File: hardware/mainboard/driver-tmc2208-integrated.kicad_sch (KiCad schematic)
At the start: 9 parts, among them M1 JST XH, U2 TMC2208-LA

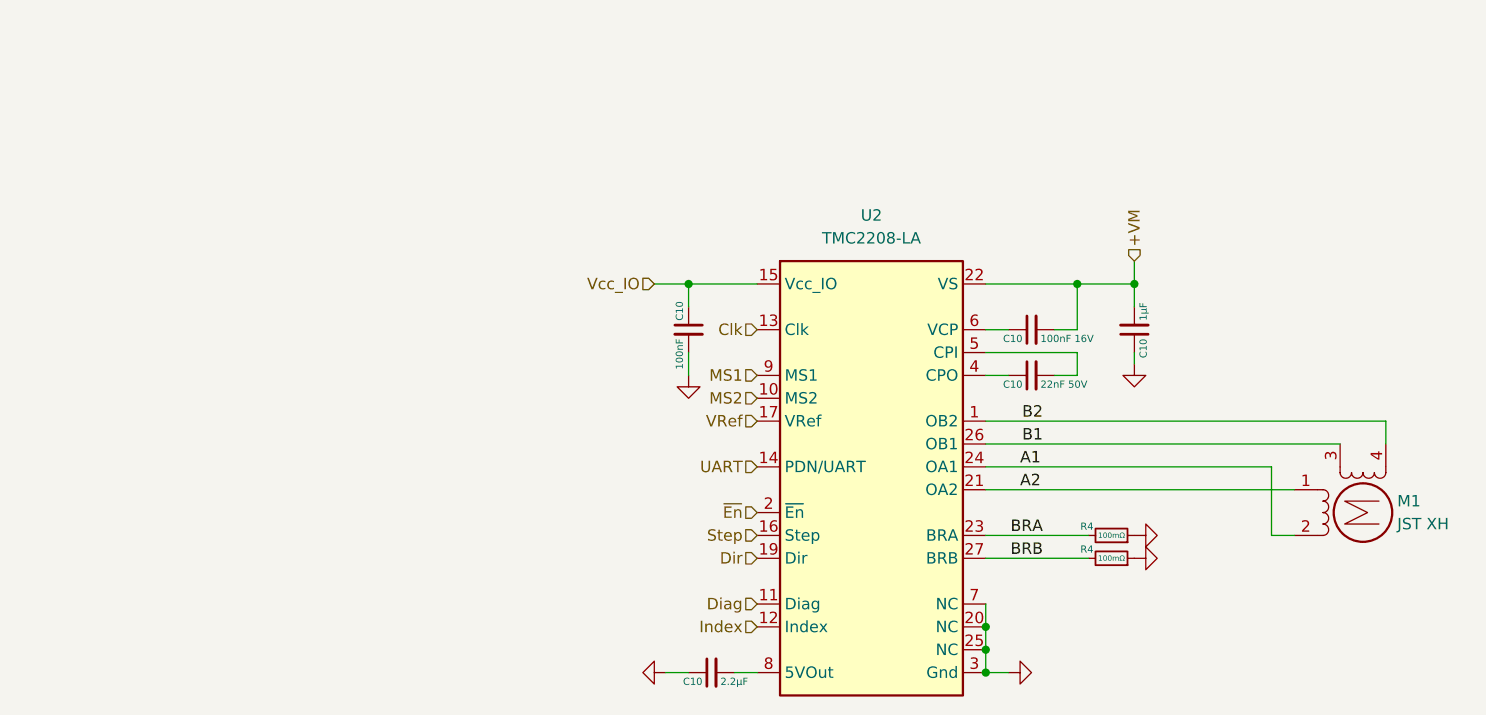
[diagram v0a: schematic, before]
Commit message: added fan / heater ports to mainboard, and footprints for switches, transistors, etc.
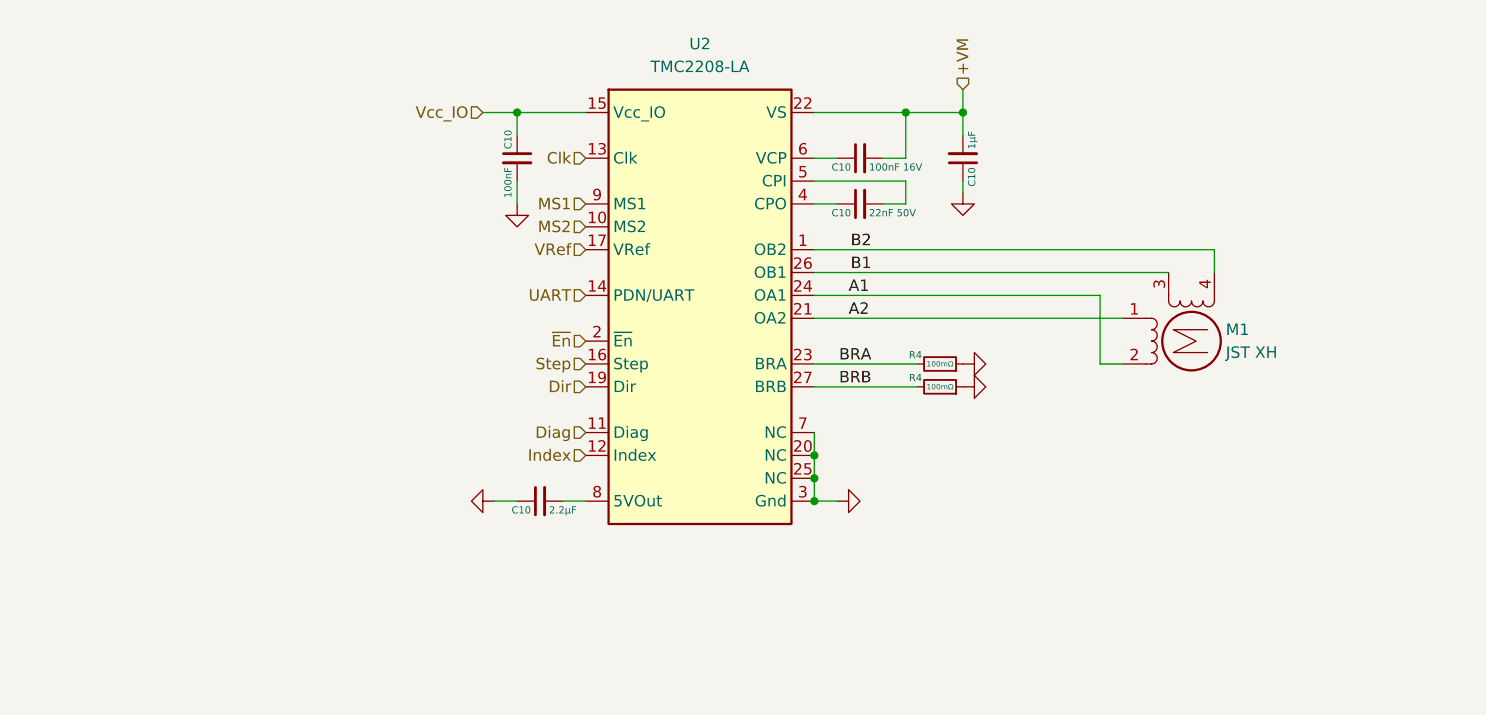
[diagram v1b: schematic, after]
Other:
- company: (none) -> Meridi Engineering
- title: (none) -> Integrated TMC2208 Driver Block
- moved on the sheet: C10, M1, R4, U2

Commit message: saving mainboard, gonna tear out the entire thing and redo in 4-layer
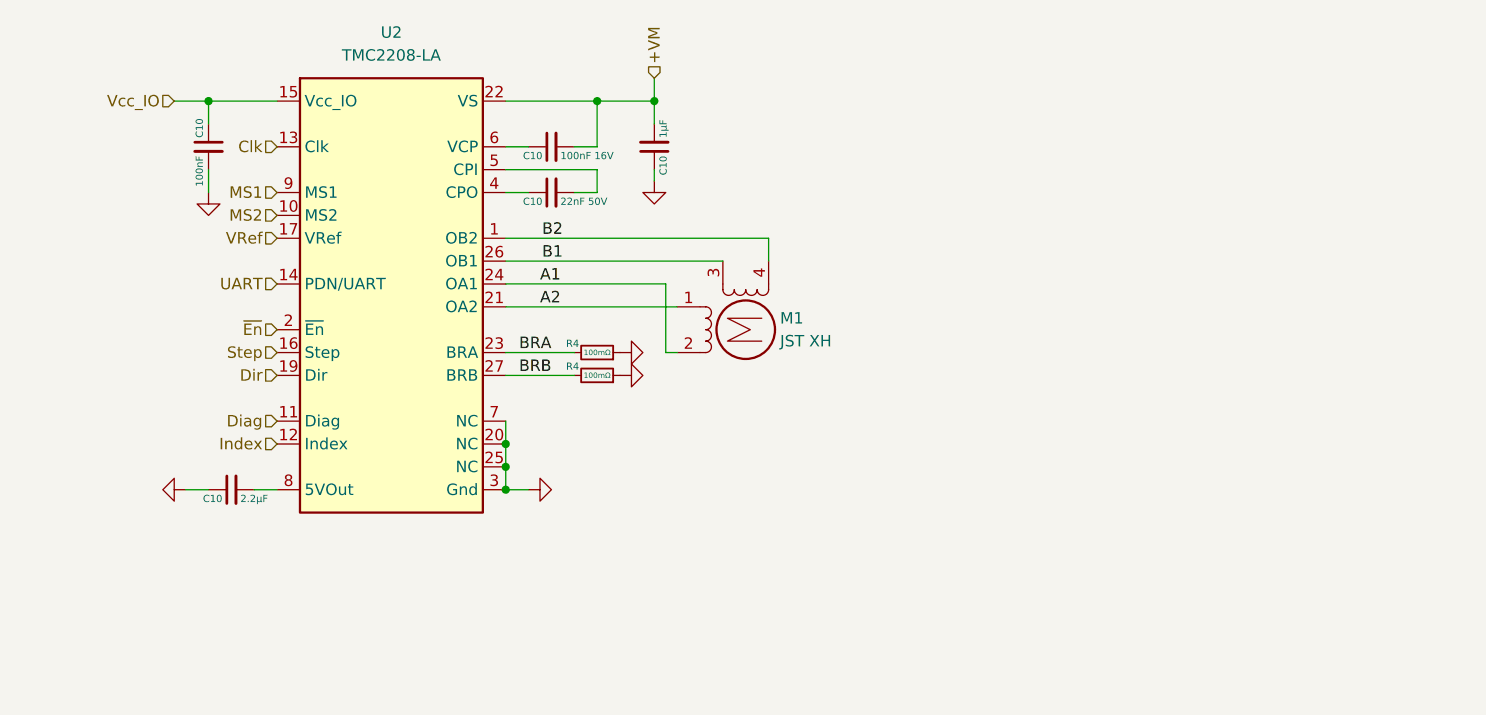
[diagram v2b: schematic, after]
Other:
- moved on the sheet: C10, M1, R4, U2

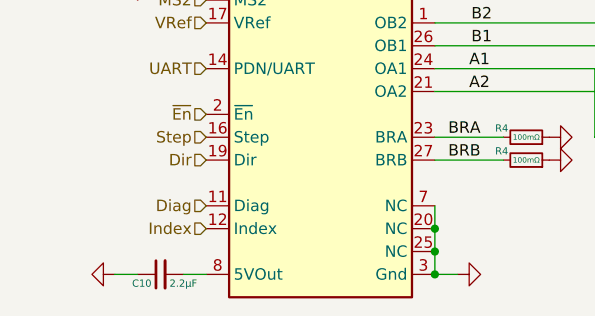
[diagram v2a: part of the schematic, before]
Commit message: further board edits, mostly done with power planes, heaters, fans, motor channels, starting work on microcontroller signals
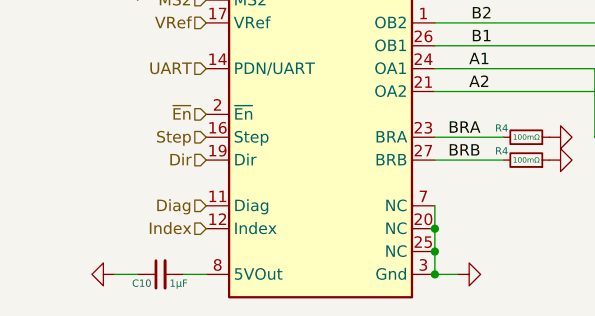
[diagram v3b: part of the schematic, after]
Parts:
- C10: value 2.2μF -> 1μF; footprint AlphaLib:0603C -> AlphaLib:0402C
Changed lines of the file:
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@@
       (effects (font (size 0.8 0.8)) (justify left))
     )
-    (property "Value" "2.2μF" (at 42.91 83.55 90)
+    (property "Value" "1μF" (at 42.91 83.55 90)
       (effects (font (size 0.8 0.8)) (justify right))
     )
-    (property "Footprint" "AlphaLib:0603C" (at 41.91 82.55 0)
+    (property "Footprint" "AlphaLib:0402C" (at 41.91 82.55 0)
       (effects (font (size 1.27 1.27)) hide)
     )

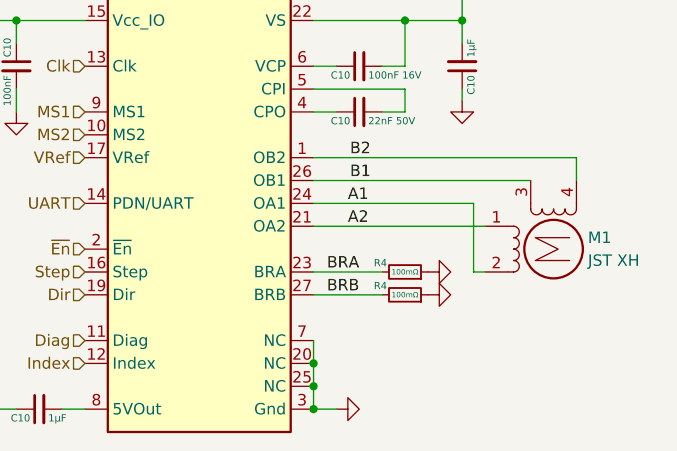
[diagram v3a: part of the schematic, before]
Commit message: redid mainboard, added probe wiring, replacing ncp chip with LM5160 for now
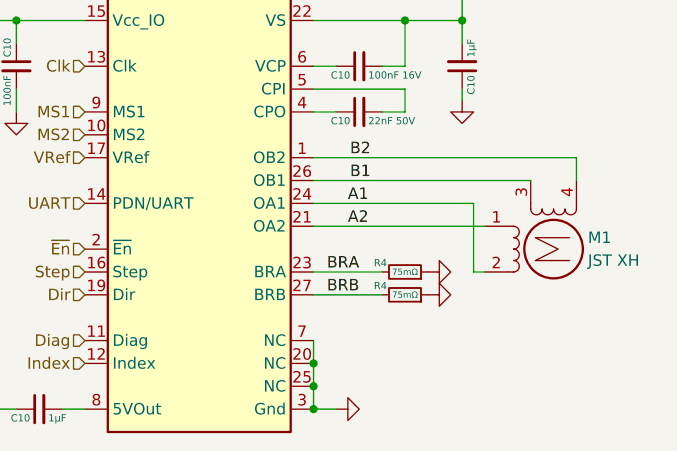
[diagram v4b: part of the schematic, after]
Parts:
- R4: value 100mΩ -> 75mΩ
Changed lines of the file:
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@@
       (effects (font (size 0.8 0.8)) (justify right))
     )
-    (property "Value" "100mΩ" (at 82.55 67.31 90)
-      (effects (font (size 0.6 0.6)))
+    (property "Value" "75mΩ" (at 82.55 67.31 90)
+      (effects (font (size 0.7 0.7)))
     )
     (property "Footprint" "Resistor_SMD:R_0805_2012Metric" (at 82.55 67.31 0)
@@
       (effects (font (size 0.8 0.8)) (justify right))
     )
-    (property "Value" "100mΩ" (at 82.55 69.85 90)
-      (effects (font (size 0.6 0.6)))
+    (property "Value" "75mΩ" (at 82.55 69.85 90)
+      (effects (font (size 0.7 0.7)))
     )
     (property "Footprint" "Resistor_SMD:R_0805_2012Metric" (at 82.55 69.85 0)

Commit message: nearing first prototype woot! copyediting over entire board, fixed some mistakes
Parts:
- added R3: 10kΩ, AlphaLib:0402R, symbol Device:R_Small
- C10: value 1μF -> 1μF 50V; footprint Capacitor_SMD:C_0805_2012Metric -> Capacitor_SMD:C_0603_1608Metric
- R4: value 75mΩ -> 100mΩ
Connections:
- net BRA: now also R4.1; no longer R4.2
- net BRB: now also R4.1; no longer R4.2
- net GND: now also R4.2, R4.2, R3.1; no longer R4.1, R4.1
- net ~{En}: now also R3.2
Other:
- moved on the sheet: M1, R4

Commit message: redoing board for version alpha 0.2
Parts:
- renumbered U2 to U7

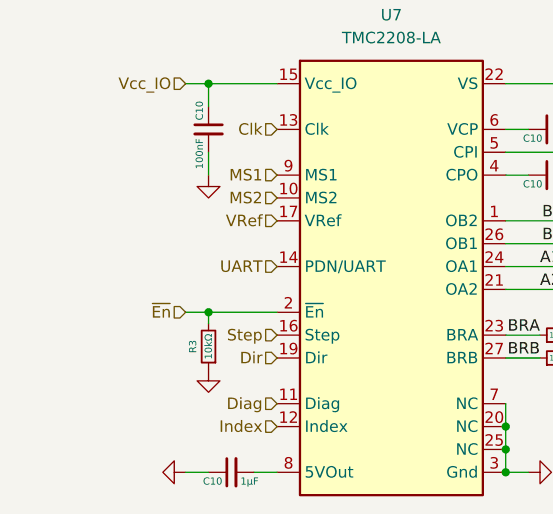
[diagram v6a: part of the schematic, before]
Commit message: tested SMD style XH connectors — didn't work very well alas
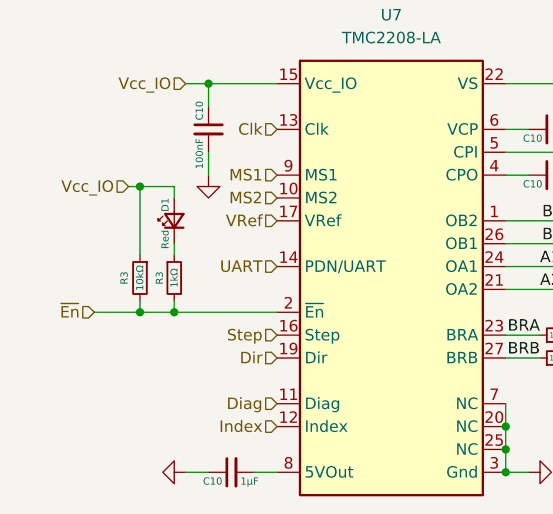
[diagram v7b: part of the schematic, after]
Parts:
- removed R3: 10kΩ, AlphaLib:0402R, symbol Device:R_Small
- added D1: Red, AlphaLib:0402LED, symbol Device:LED_Small
- added R3: 1kΩ, AlphaLib:0402R, symbol Device:R_Small
- added R3: 10kΩ, AlphaLib:0402R, symbol Device:R_Small
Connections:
- net Vcc_IO: now also D1.2 (A), R3.1
- net ~{En}: now also R3.2, R3.2
- new net: D1.1 (K), R3.1

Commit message: fan ports
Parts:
- removed R3: 10kΩ, AlphaLib:0402R, symbol Device:R_Small
- C10: footprint Capacitor_SMD:C_0603_1608Metric -> AlphaLib:0603C
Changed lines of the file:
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@@
   (junction (at 88.9 39.37) (diameter 0) (color 0 0 0 0)
   )
-  (junction (at 31.75 50.8) (diameter 0) (color 0 0 0 0)
-  )
   (junction (at 82.55 39.37) (diameter 0) (color 0 0 0 0)
   )
@@
   (junction (at 72.39 82.55) (diameter 0) (color 0 0 0 0)
   )
-  (junction (at 31.75 64.77) (diameter 0) (color 0 0 0 0)
-  )
   (wire (pts (xy 72.39 49.53) (xy 74.93 49.53))
     (stroke (width 0) (type default))
@@
     (stroke (width 0) (type default))
   )
-  (wire (pts (xy 26.67 64.77) (xy 31.75 64.77))
+  (wire (pts (xy 26.67 64.77) (xy 35.56 64.77))
     (stroke (width 0) (type default))
   )
@@
     (stroke (width 0) (type default))
   )
-  (wire (pts (xy 31.75 50.8) (xy 31.75 58.42))
-    (stroke (width 0) (type default))
-  )
   (wire (pts (xy 72.39 54.61) (xy 97.79 54.61))
     (stroke (width 0) (type default))
   )
-  (wire (pts (xy 35.56 64.77) (xy 31.75 64.77))
-    (stroke (width 0) (type default))
-  )
-  (wire (pts (xy 31.75 50.8) (xy 35.56 50.8))
+  (wire (pts (xy 30.48 50.8) (xy 35.56 50.8))
     (stroke (width 0) (type default))
   )
@@
     (stroke (width 0) (type default))
   )
-  (wire (pts (xy 31.75 63.5) (xy 31.75 64.77))
-    (stroke (width 0) (type default))
-  )
   (wire (pts (xy 80.01 49.53) (xy 82.55 49.53))
     (stroke (width 0) (type default))
@@
   )
   (wire (pts (xy 81.28 67.31) (xy 82.55 67.31))
-    (stroke (width 0) (type default))
-  )
-  (wire (pts (xy 30.48 50.8) (xy 31.75 50.8))
     (stroke (width 0) (type default))
   )
@@
     )
   )
-  (symbol (lib_id "Device:R_Small") (at 31.75 60.96 0) (mirror y) (unit 1)
-    (in_bom yes) (on_board yes) (dnp no)
-    (property "Reference" "R3" (at 30.48 60.96 90)
-      (effects (font (size 0.8 0.8)) (justify top))
-    )
-    (property "Value" "10kΩ" (at 31.75 60.96 90)
-      (effects (font (size 0.8 0.8)))
-    )
-    (property "Footprint" "AlphaLib:0402R" (at 31.75 60.96 0)
-      (effects (font (size 1.27 1.27)) hide)
-    )
-    (property "Datasheet" "~" (at 31.75 60.96 0)
-      (effects (font (size 1.27 1.27)) hide)
-    )
-    (pin "1")
-    (pin "2")
-    (instances
-      (project "driver-tmc5160"
-        (path "/03364e55-5655-494a-997e-0cd456c2d9b5"
-          (reference "R3") (unit 1)
-        )
-      )
-      (project "mainboard"
-        (path "/1a565782-f217-442e-b118-196625f31c53"
-          (reference "R104") (unit 1)
-        )
-        (path "/1a565782-f217-442e-b118-196625f31c53/972ca71f-1c40-4278-8cb4-2b520c3e8975"
-          (reference "R19") (unit 1)
-        )
-        (path "/1a565782-f217-442e-b118-196625f31c53/99778979-7977-44ff-ba7b-f489010f8682"
-          (reference "R25") (unit 1)
-        )
-        (path "/1a565782-f217-442e-b118-196625f31c53/f6e6a5bb-7803-4b0b-883d-433919711a15"
-          (reference "R100") (unit 1)
-        )
-        (path "/1a565782-f217-442e-b118-196625f31c53/64a332d7-9292-493c-af4b-24f0e80d7999"
-          (reference "R102") (unit 1)
-        )
-        (path "/1a565782-f217-442e-b118-196625f31c53/09bb4a8f-8694-4b82-8e1f-fabe3bd11ec7"
-          (reference "R31") (unit 1)
-        )
-        (path "/1a565782-f217-442e-b118-196625f31c53/d34aeff3-da22-4edc-92e0-1591d6117dbc"
-          (reference "R39") (unit 1)
-        )
-      )
-    )
-  )
   (symbol (lib_id "power:GND") (at 82.55 67.31 90) (unit 1)
     (in_bom yes) (on_board yes) (dnp no) (fields_autoplaced)
@@
       (effects (font (size 0.8 0.8)) (justify right))
     )
-    (property "Footprint" "Capacitor_SMD:C_0603_1608Metric" (at 88.9 44.45 0)
-      (effects (font (size 1.27 1.27)) hide)
-    )
+    (property "Footprint" "AlphaLib:0603C" (at 88.9 44.45 0)
+      (effects (font (size 1.27 1.27)) hide)
+    )
